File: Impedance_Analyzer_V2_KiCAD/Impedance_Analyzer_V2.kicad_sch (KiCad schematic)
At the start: 51 parts, among them J1 Conn_Coaxial, J10 Conn_02x02_Counter_Clockwise, J11 Screw_Terminal_01x03, J12 Conn_02x02_Counter_Clockwise, J13 Conn_02x02_Counter_Clockwise, J14 Conn_02x02_Counter_Clockwise, J15 Conn_02x02_Counter_Clockwise, J16 Conn_02x02_Counter_Clockwise, J17 Conn_02x02_Counter_Clockwise, J2 Conn_Coaxial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

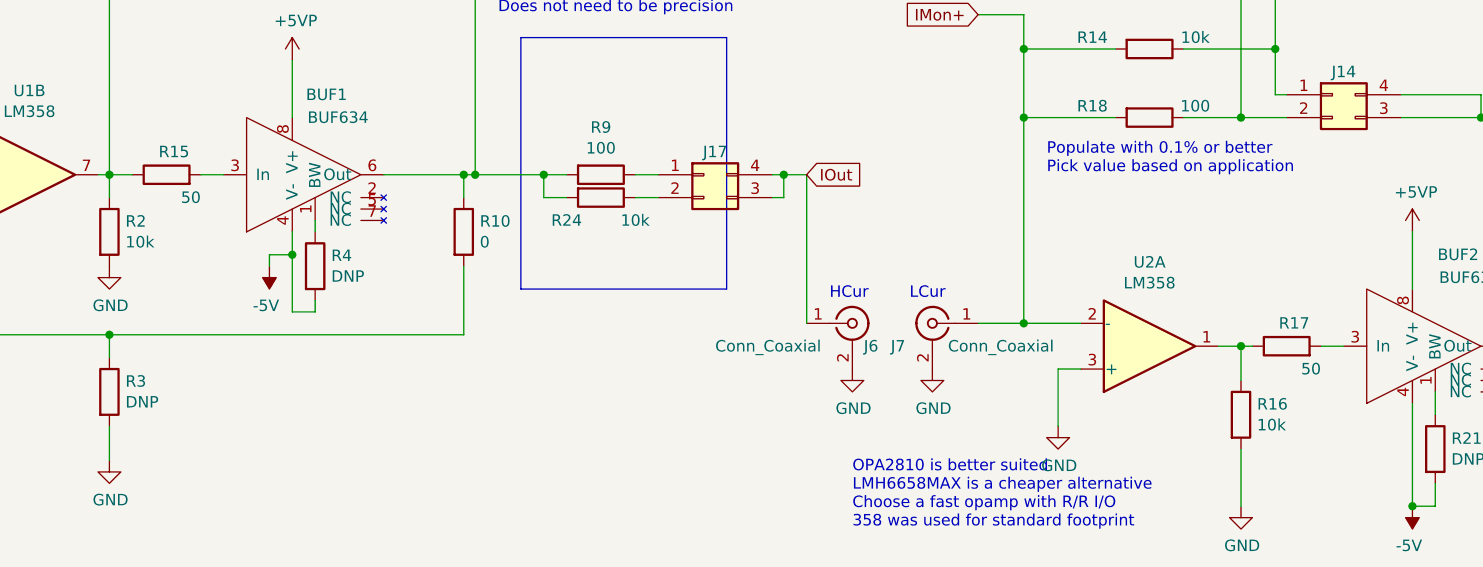
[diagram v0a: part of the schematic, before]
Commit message: Add STEP file, minor changes
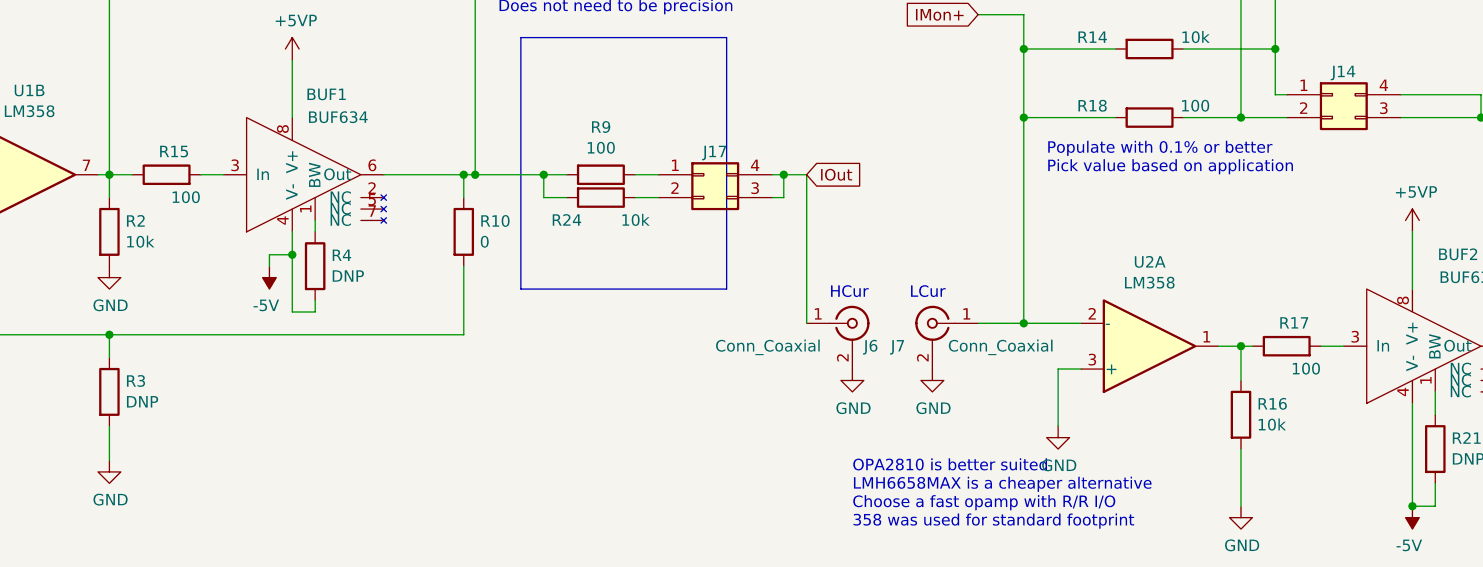
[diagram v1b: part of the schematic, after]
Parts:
- R15, R17: value 50 -> 100
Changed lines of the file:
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@@
       (effects (font (size 1.27 1.27)) (justify left))
     )
-    (property "Value" "50" (id 1) (at 113.03 57.15 90)
+    (property "Value" "100" (id 1) (at 113.03 57.15 90)
       (effects (font (size 1.27 1.27)) (justify left))
     )
@@
       (effects (font (size 1.27 1.27)) (justify left))
     )
-    (property "Value" "50" (id 1) (at 237.49 76.2 90)
+    (property "Value" "100" (id 1) (at 237.49 76.2 90)
       (effects (font (size 1.27 1.27)) (justify left))
     )
@@
     )
     (path "/753e6bfa-d8cb-4636-9cc1-37c0acfdfb21"
-      (reference "R15") (unit 1) (value "50") (footprint "Resistor_SMD:R_1206_3216Metric")
+      (reference "R15") (unit 1) (value "100") (footprint "Resistor_SMD:R_1206_3216Metric")
     )
     (path "/7927dbc1-ff57-4dce-a8fb-824e25958252"
@@
     )
     (path "/ac61a9b4-2268-4b14-a597-ed5765e1c67d"
-      (reference "R17") (unit 1) (value "50") (footprint "Resistor_SMD:R_1206_3216Metric")
+      (reference "R17") (unit 1) (value "100") (footprint "Resistor_SMD:R_1206_3216Metric")
     )
     (path "/00000000-0000-0000-0000-000061c820b5"
